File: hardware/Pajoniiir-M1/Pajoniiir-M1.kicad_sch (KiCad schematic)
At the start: 0 parts

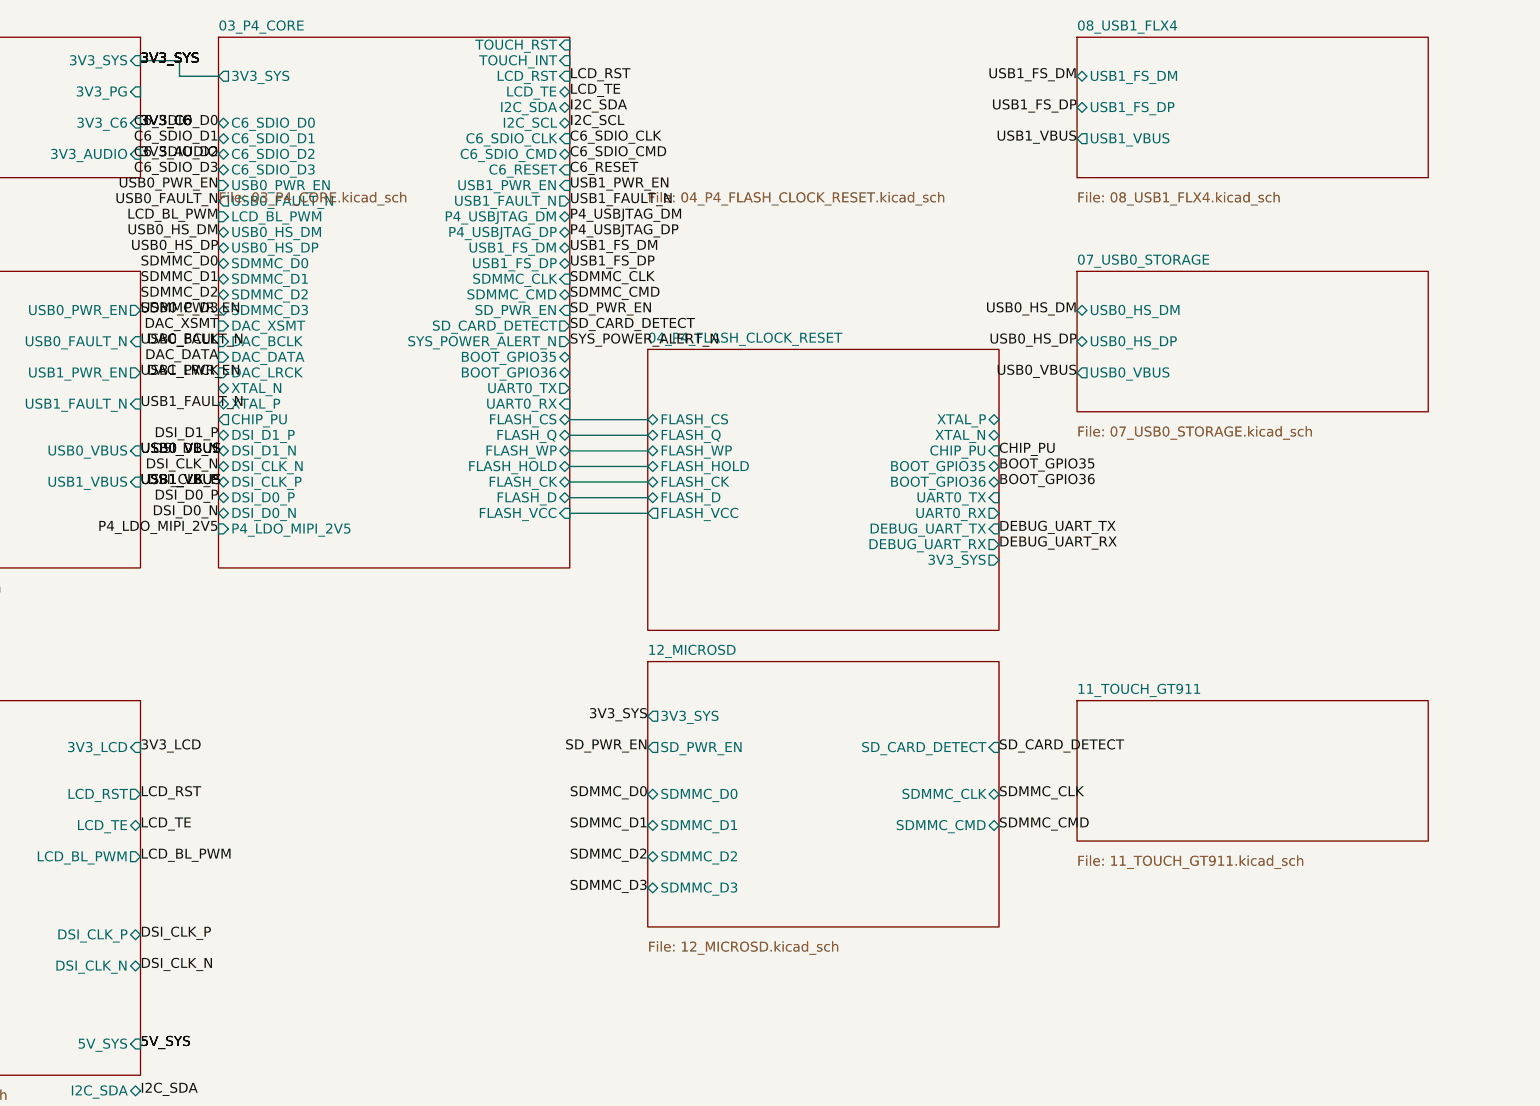
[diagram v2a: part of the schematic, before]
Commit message: hardware: wire GT911 touch hierarchy
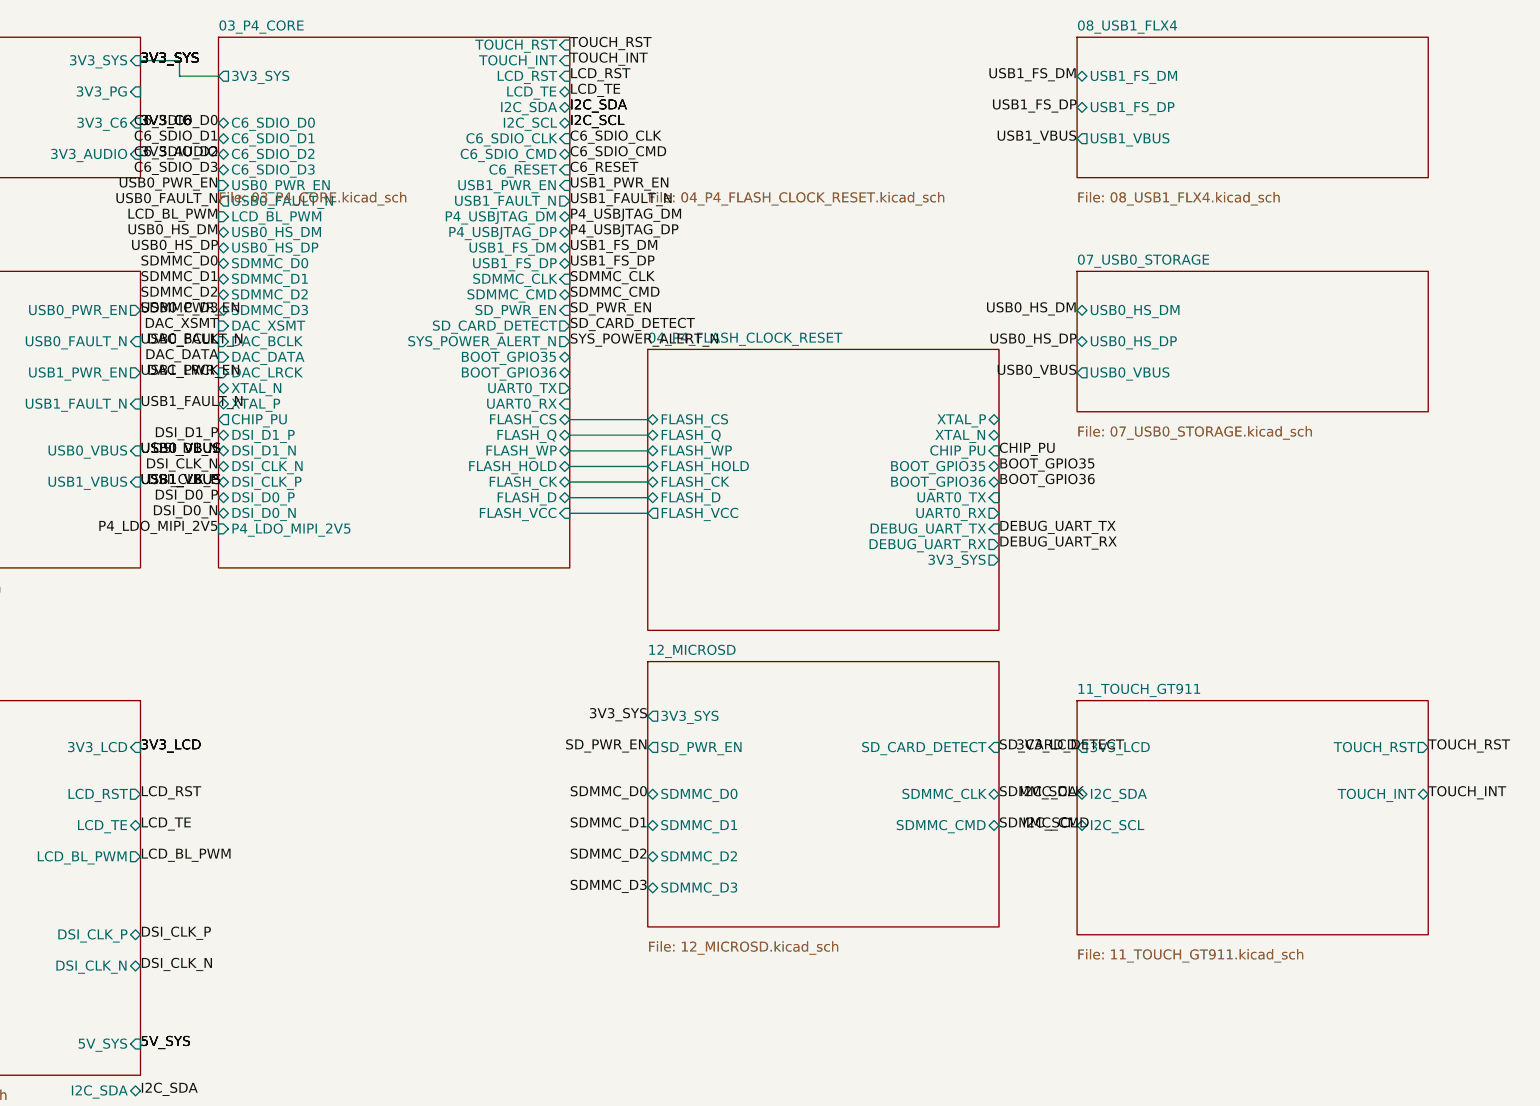
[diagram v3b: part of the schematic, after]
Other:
- sheet 11_TOUCH_GT911 ports: added 3V3_LCD, I2C_SCL, I2C_SDA, TOUCH_INT, TOUCH_RST; removed none
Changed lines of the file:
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@@
   (sheet
     (at 240 105)
-    (size 45 18)
+    (size 45 30)
     (fields_autoplaced yes)
     (stroke (width 0.1524) (type solid))
@@
     )
     (property "Sheetfile" "11_TOUCH_GT911.kicad_sch"
-      (at 240 124.8246 0)
-      (effects (font (size 1.27 1.27)) (justify left top))
-    )
+      (at 240 136.8246 0)
+      (effects (font (size 1.27 1.27)) (justify left top))
+    )
+    (pin "3V3_LCD" output (at 240 111 180) (effects (font (size 1.27 1.27)) (justify left)))
+    (pin "I2C_SDA" bidirectional (at 240 117 180) (effects (font (size 1.27 1.27)) (justify left)))
+    (pin "I2C_SCL" bidirectional (at 240 121 180) (effects (font (size 1.27 1.27)) (justify left)))
+    (pin "TOUCH_RST" output (at 285 111 0) (effects (font (size 1.27 1.27)) (justify right)))
+    (pin "TOUCH_INT" bidirectional (at 285 117 0) (effects (font (size 1.27 1.27)) (justify right)))
     (instances
       (project "Pajoniiir-M1"
@@
   (label "DSI_D0_P" (at 130 79 180) (effects (font (size 1.27 1.27))))
   (label "DSI_D0_N" (at 130 81 180) (effects (font (size 1.27 1.27))))
+  (label "3V3_LCD" (at 240 111 180) (effects (font (size 1.27 1.27))))
+  (label "I2C_SDA" (at 240 117 180) (effects (font (size 1.27 1.27))))
+  (label "I2C_SCL" (at 240 121 180) (effects (font (size 1.27 1.27))))
+  (label "TOUCH_RST" (at 285 111 0) (effects (font (size 1.27 1.27))))
+  (label "TOUCH_INT" (at 285 117 0) (effects (font (size 1.27 1.27))))
+  (label "3V3_LCD" (at 120 111 0) (effects (font (size 1.27 1.27))))
+  (label "I2C_SDA" (at 175 29 0) (effects (font (size 1.27 1.27))))
+  (label "I2C_SCL" (at 175 31 0) (effects (font (size 1.27 1.27))))
+  (label "TOUCH_RST" (at 175 21 0) (effects (font (size 1.27 1.27))))
+  (label "TOUCH_INT" (at 175 23 0) (effects (font (size 1.27 1.27))))
   (sheet_instances (path "/" (page "1")))
   (embedded_fonts no)
